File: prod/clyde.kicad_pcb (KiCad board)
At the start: 2 copper layers, 111.4 x 85.7 mm, 26 parts

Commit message: prototypes ordered
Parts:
- removed the G*** at (196.5, 151.8)
- removed the G*** at (196.4, 151.3)
- added G***: LOGO, main:north-sky-silk, F.Cu at (198.8, 149.9)
- added G***: LOGO, main:north-sky-silk, B.Cu at (198.8, 149.9)
- moved S16 1.91 mm to (206.7, 179.1)
- moved S17 1.91 mm to (225.7, 179.1)
- moved _4 1.91 mm to (235.3, 169.5)
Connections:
- TRRS1 pad 4: GP12 -> GP16
- U0 pad 10: matrix_middle_home -> matrix_inner_home
- U0 pad 11: matrix_middle_bottom -> matrix_inner_bottom
- U0 pad 12: matrix_index_top -> matrix_ring_bottom
- U0 pad 14: matrix_index_home -> matrix_ring_home
- U0 pad 15: matrix_index_bottom -> matrix_ring_top
- U0 pad 16: GP12 -> matrix_middle_top
- U0 pad 17: matrix_inner_bottom -> matrix_middle_home
- U0 pad 19: matrix_inner_home -> matrix_middle_bottom
- U0 pad 20: matrix_inner_top -> GP15
- U0 pad 21: thumbfan_far_home -> GP16
- U0 pad 22: thumbfan_home_home -> thumbfan_far_home
- U0 pad 24: thumbfan_near_home -> thumbfan_home_home
- U0 pad 25: GP19 -> thumbfan_near_home
- U0 pad 5: matrix_ring_bottom -> matrix_index_bottom
- U0 pad 6: matrix_ring_home -> matrix_index_home
- U0 pad 7: matrix_ring_top -> matrix_index_top
- U0 pad 9: matrix_middle_top -> matrix_inner_top
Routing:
- net GP16: track 0.00 -> 117.3 mm
- net GP12: track 114.2 -> 0.00 mm, vias 2 -> 0
- net matrix_inner_top: track 105.9 -> 140.8 mm
- net matrix_index_bottom: track 45.5 -> 78.3 mm
- net matrix_index_home: track 65.8 -> 93.8 mm, vias 2 -> 1
- net matrix_inner_home: track 90.1 -> 116.3 mm, vias 0 -> 1
- net thumbfan_far_home: track 107.0 -> 81.8 mm
- net matrix_ring_home: track 67.2 -> 48.4 mm
- net matrix_ring_bottom: track 50.1 -> 31.3 mm
- net matrix_inner_bottom: track 74.2 -> 92.9 mm, vias 0 -> 1
- net matrix_ring_top: track 84.2 -> 66.4 mm
- net matrix_index_top: track 90.6 -> 107.7 mm
- net thumbfan_home_home: track 78.5 -> 65.0 mm
- net matrix_middle_top: track 78.1 -> 66.6 mm
- net matrix_middle_home: track 57.2 -> 50.1 mm
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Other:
- outline, holes or cut-outs redrawn

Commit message: layout like split weteor/Kong; outline tweaks
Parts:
- removed the G*** at (198.8, 149.9) (x2)
- added G***: LOGO, main:north-sky-silk, F.Cu at (197.2, 151.8)
- added G***: LOGO, main:north-sky-silk, B.Cu at (197.0, 151.8)
- moved S16 4.76 mm to (209.6, 175.3)
- moved S17 4.76 mm to (228.6, 175.3)
- moved _4 4.76 mm to (238.1, 165.7)
- moved S18 4.39 mm to (247.7, 177.6)
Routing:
- net thumbfan_home_home: track 65.0 -> 88.8 mm
- net thumbfan_far_home: track 81.8 -> 95.3 mm
- net matrix_inner_bottom: track 92.9 -> 104.9 mm
- net matrix_index_top: track 107.7 -> 117.8 mm
- net matrix_inner_home: track 116.3 -> 124.6 mm
- net matrix_inner_top: track 140.8 -> 146.5 mm
- net matrix_index_home: track 93.8 -> 99.1 mm
- net thumbfan_near_home: track 67.8 -> 71.8 mm
- net matrix_ring_bottom: track 31.3 -> 35.3 mm
- net matrix_index_bottom: track 78.3 -> 81.8 mm
- net matrix_middle_top: track 66.6 -> 68.5 mm
- net matrix_middle_home: track 50.1 -> 48.5 mm
- net matrix_pinky_top: track 64.0 -> 65.4 mm
- net matrix_ring_top: track 66.4 -> 67.7 mm
- net matrix_middle_bottom: track 33.5 -> 34.7 mm
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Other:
- board size 111.4 x 85.7 mm -> 114.3 x 82.4 mm
- board text added: "clyde v0.0.2"
- board text removed: "clyde v0.0.1"

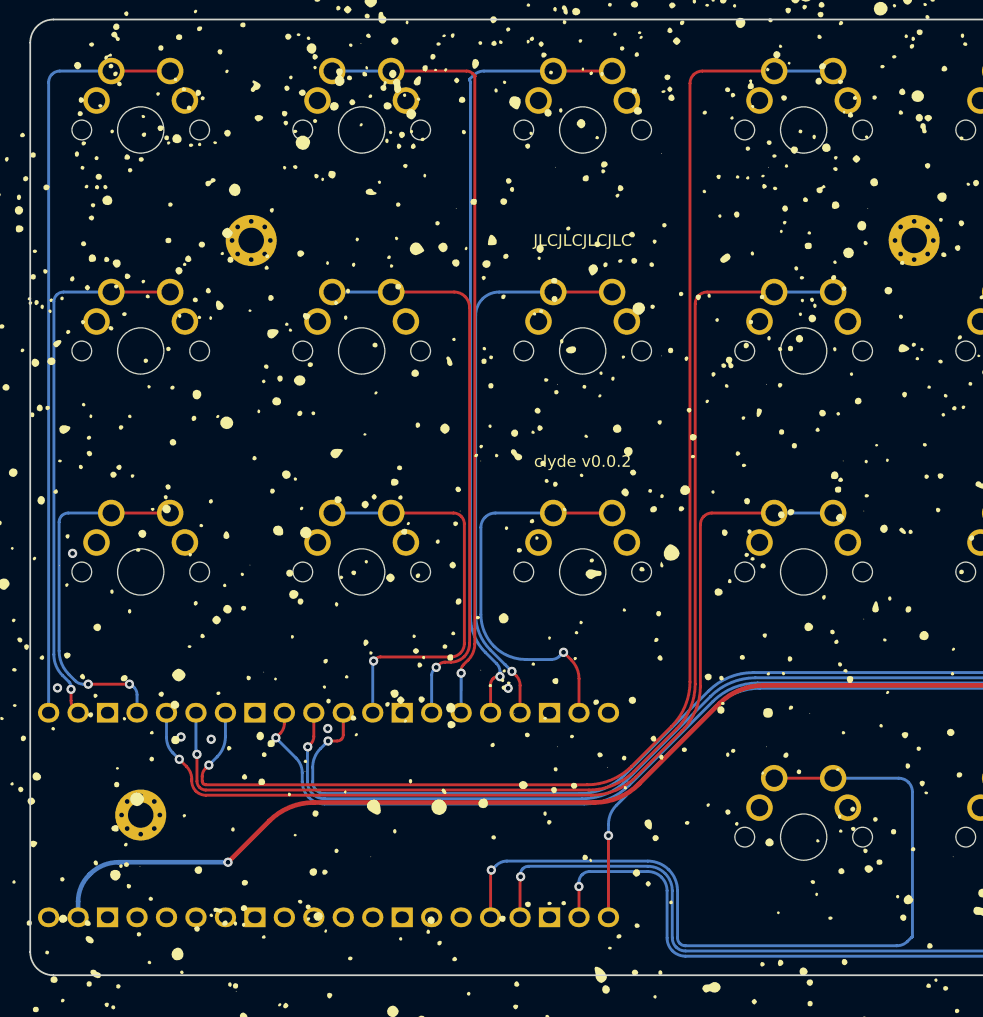
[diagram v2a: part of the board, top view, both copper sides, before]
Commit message: fix some routing irregularities
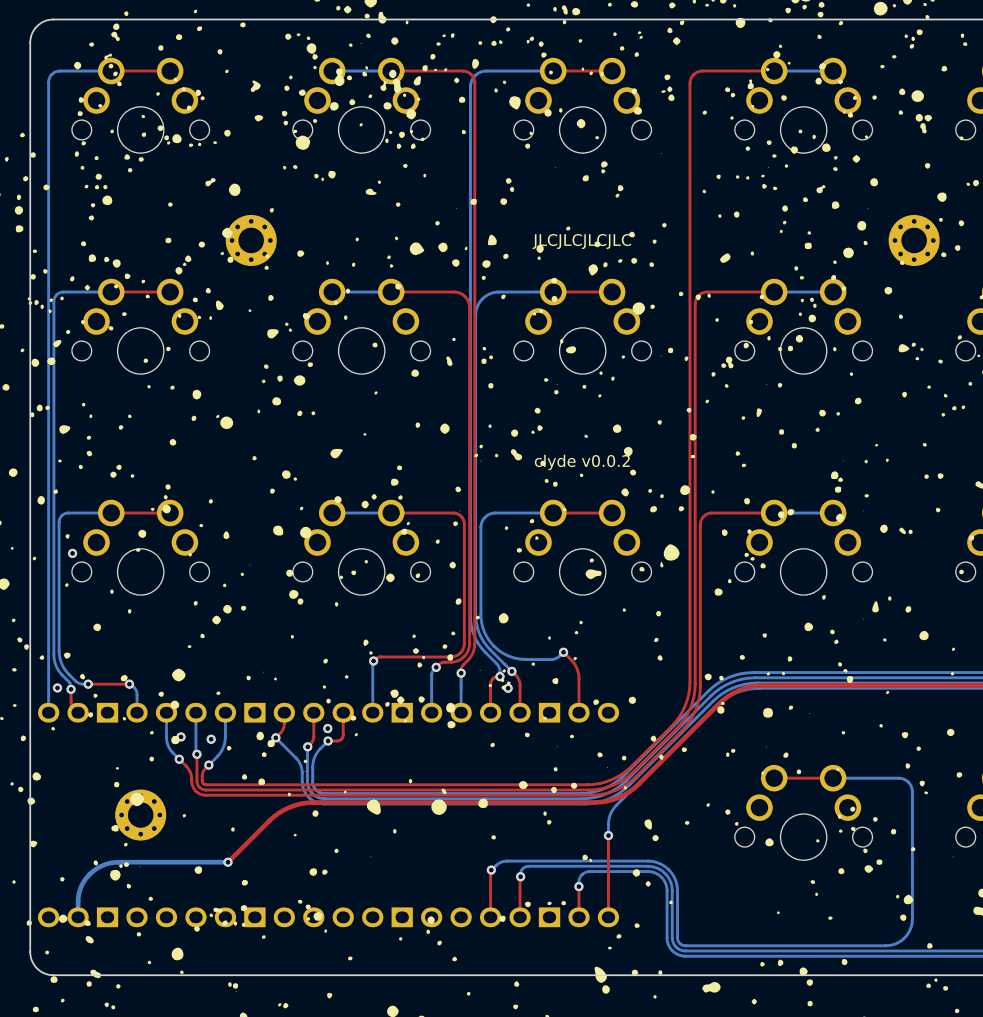
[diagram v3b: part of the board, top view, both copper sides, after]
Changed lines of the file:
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@@
   (segment (start 146.39375 162.51875) (end 146.39375 163.495798) (width 0.25) (layer "F.Cu") (net 3))
   (via (at 146.39375 162.51875) (size 0.8) (drill 0.4) (layers "F.Cu" "B.Cu") (net 3))
-  (arc (start 146.698125 164.230625) (mid 146.472854 163.893483) (end 146.39375 163.495798) (width 0.25) (layer "F.Cu") (net 3))
+  (arc (start 146.39375 163.495798) (mid 146.472854 163.893483) (end 146.698125 164.230625) (width 0.25) (layer "F.Cu") (net 3))
   (segment (start 146.39375 162.2875) (end 146.39375 162.51875) (width 0.25) (layer "B.Cu") (net 3))
   (segment (start 146.230231 161.892731) (end 145.653125 161.315625) (width 0.25) (layer "B.Cu") (net 3))
@@
   (segment (start 168.91 128.27) (end 173.99 128.27) (width 0.25) (layer "B.Cu") (net 6))
   (arc (start 177.67875 160.82125) (mid 177.533503 161.038626) (end 177.4825 161.295039) (width 0.25) (layer "B.Cu") (net 6))
+  (segment (start 180.1672 109.22) (end 173.99 109.22) (width 0.25) (layer "F.Cu") (net 7))
+  (segment (start 181.2 110.252799) (end 181.2 158.591941) (width 0.25) (layer "F.Cu") (net 7))
   (segment (start 180.612499 160.010291) (end 180.211396 160.411395) (width 0.25) (layer "F.Cu") (net 7))
-  (segment (start 181.2125 109.6375) (end 181.01 109.435) (width 0.25) (layer "F.Cu") (net 7))
-  (segment (start 181.2 109.692677) (end 181.2 158.591941) (width 0.25) (layer "F.Cu") (net 7))
   (segment (start 180.025 160.861396) (end 180.025 161.125) (width 0.25) (layer "F.Cu") (net 7))
-  (segment (start 180.490944 109.22) (end 173.99 109.22) (width 0.25) (layer "F.Cu") (net 7))
   (via (at 180.025 161.125) (size 0.8) (drill 0.4) (layers "F.Cu" "B.Cu") (net 7))
+  (arc (start 180.8975 109.5225) (mid 180.562435 109.298617) (end 180.1672 109.22) (width 0.25) (layer "F.Cu") (net 7))
+  (arc (start 180.211396 160.411395) (mid 180.073442 160.617857) (end 180.025 160.861396) (width 0.25) (layer "F.Cu") (net 7))
   (arc (start 180.612499 160.010291) (mid 181.047313 159.359546) (end 181.2 158.591941) (width 0.25) (layer "F.Cu") (net 7))
-  (arc (start 181.2125 109.6375) (mid 181.217677 109.65) (end 181.2125 109.6625) (width 0.25) (layer "F.Cu") (net 7))
-  (arc (start 180.211396 160.411395) (mid 180.073442 160.617857) (end 180.025 160.861396) (width 0.25) (layer "F.Cu") (net 7))
-  (arc (start 181.01 109.435) (mid 180.771855 109.275876) (end 180.490944 109.22) (width 0.25) (layer "F.Cu") (net 7))
-  (arc (start 181.2 109.692677) (mid 181.203248 109.676345) (end 181.2125 109.6625) (width 0.25) (layer "F.Cu") (net 7))
+  (arc (start 181.2 110.252799) (mid 181.121382 109.857564) (end 180.8975 109.5225) (width 0.25) (layer "F.Cu") (net 7))
   (segment (start 168.91 109.22) (end 173.99 109.22) (width 0.25) (layer "B.Cu") (net 7))
   (segment (start 180.025 161.125) (end 180.0225 164.535) (width 0.25) (layer "B.Cu") (net 7))
@@
   (arc (start 182.5625 162.086503) (mid 182.612853 161.833356) (end 182.756249 161.618749) (width 0.25) (layer "F.Cu") (net 10))
   (segment (start 182.1 159.322792) (end 183.082537 160.305329) (width 0.25) (layer "B.Cu") (net 10))
-  (segment (start 180.7625 109.9125) (end 181.0775 109.5975) (width 0.25) (layer "B.Cu") (net 10))
-  (segment (start 180.825 156.244669) (end 180.825 110.188388) (width 0.25) (layer "B.Cu") (net 10))
-  (segment (start 181.988865 109.22) (end 187.96 109.22) (width 0.25) (layer "B.Cu") (net 10))
+  (segment (start 180.825 110.60027) (end 180.825 156.244669) (width 0.25) (layer "B.Cu") (net 10))
   (segment (start 183.375 161.011396) (end 183.375 161.425) (width 0.25) (layer "B.Cu") (net 10))
-  (arc (start 181.988865 109.22) (mid 181.495637 109.318109) (end 181.0775 109.5975) (width 0.25) (layer "B.Cu") (net 10))
-  (arc (start 180.7625 109.9125) (mid 180.736611 109.975) (end 180.7625 110.0375) (width 0.25) (layer "B.Cu") (net 10))
-  (arc (start 180.7625 110.0375) (mid 180.808756 110.106728) (end 180.825 110.188388) (width 0.25) (layer "B.Cu") (net 10))
+  (segment (start 182.20527 109.22) (end 187.96 109.22) (width 0.25) (layer "B.Cu") (net 10))
   (arc (start 180.825 156.244669) (mid 181.156361 157.910537) (end 182.1 159.322792) (width 0.25) (layer "B.Cu") (net 10))
+  (arc (start 180.825 110.60027) (mid 180.930066 110.072063) (end 181.229272 109.624272) (width 0.25) (layer "B.Cu") (net 10))
   (arc (start 183.375 161.011396) (mid 183.298991 160.629275) (end 183.082537 160.305329) (width 0.25) (layer "B.Cu") (net 10))
+  (arc (start 181.229272 109.624272) (mid 181.677063 109.325066) (end 182.20527 109.22) (width 0.25) (layer "B.Cu") (net 10))
   (segment (start 158.018198 171.65) (end 191.246036 171.65) (width 0.25) (layer "F.Cu") (net 11))
   (segment (start 156.8 170.280698) (end 156.8 170.431801) (width 0.25) (layer "F.Cu") (net 11))
@@
   (via (at 182.625 178.1) (size 0.8) (drill 0.4) (layers "F.Cu" "B.Cu") (net 17))
   (arc (start 182.5625 178.206694) (mid 182.570621 178.165864) (end 182.59375 178.13125) (width 0.25) (layer "F.Cu") (net 17))
-  (segment (start 218.9125 183.8375) (end 218.910937 183.839062) (width 0.25) (layer "B.Cu") (net 17))
-  (segment (start 218.881249 183.868749) (end 218.879687 183.870312) (width 0.25) (layer "B.Cu") (net 17))
-  (segment (start 218.90625 183.84375) (end 218.9 183.85) (width 0.25) (layer "B.Cu") (net 17))
-  (segment (start 218.925 171.366439) (end 218.925 183.807322) (width 0.25) (layer "B.Cu") (net 17))
-  (segment (start 218.5125 184.2375) (end 218.8375 183.9125) (width 0.25) (layer "B.Cu") (net 17))
-  (segment (start 218.910937 183.839062) (end 218.907812 183.842187) (width 0.25) (layer "B.Cu") (net 17))
-  (segment (start 218.862499 183.887499) (end 218.870312 183.879687) (width 0.25) (layer "B.Cu") (net 17))
-  (segment (start 218.907812 183.842187) (end 218.90625 183.84375) (width 0.25) (layer "B.Cu") (net 17))
-  (segment (start 218.9 183.85) (end 218.89375 183.85625) (width 0.25) (layer "B.Cu") (net 17))
+  (segment (start 183.0375 177.7125) (end 182.65 178.1) (width 0.25) (layer "B.Cu") (net 17))
+  (segment (start 196.114339 177.325) (end 183.973007 177.325) (width 0.25) (layer "B.Cu") (net 17))
+  (segment (start 216.623806 184.625) (end 199.357842 184.625) (width 0.25) (layer "B.Cu") (net 17))
+  (segment (start 198.675 183.942157) (end 198.675 179.88566) (width 0.25) (layer "B.Cu") (net 17))
   (segment (start 217.73856 170.18) (end 212.09 170.18) (width 0.25) (layer "B.Cu") (net 17))
-  (segment (start 218.8875 183.8625) (end 218.881249 183.868749) (width 0.25) (layer "B.Cu") (net 17))
-  (segment (start 218.879687 183.870312) (end 218.870312 183.879687) (width 0.25) (layer "B.Cu") (net 17))
-  (segment (start 218.862499 183.887499) (end 218.8375 183.9125) (width 0.25) (layer "B.Cu") (net 17))
-  (segment (start 218.89375 183.85625) (end 218.8875 183.8625) (width 0.25) (layer "B.Cu") (net 17))
-  (segment (start 196.114339 177.325) (end 183.973007 177.325) (width 0.25) (layer "B.Cu") (net 17))
-  (segment (start 198.675 183.942157) (end 198.675 179.88566) (width 0.25) (layer "B.Cu") (net 17))
-  (segment (start 217.576992 184.625) (end 199.357842 184.625) (width 0.25) (layer "B.Cu") (net 17))
-  (segment (start 183.0375 177.7125) (end 182.65 178.1) (width 0.25) (layer "B.Cu") (net 17))
+  (segment (start 218.925 171.366439) (end 218.925 182.323806) (width 0.25) (layer "B.Cu") (net 17))
   (arc (start 196.114339 177.325) (mid 197.094261 177.519918) (end 197.925 178.075) (width 0.25) (layer "B.Cu") (net 17))
-  (arc (start 183.0375 177.7125) (mid 183.466714 177.425707) (end 183.973007 177.325) (width 0.25) (layer "B.Cu") (net 17))
-  (arc (start 218.5125 184.2375) (mid 218.083285 184.524292) (end 217.576992 184.625) (width 0.25) (layer "B.Cu") (net 17))
+  (arc (start 198.875 184.425) (mid 198.726978 184.203469) (end 198.675 183.942157) (width 0.25) (layer "B.Cu") (net 17))
+  (arc (start 218.250996 183.950996) (mid 217.504434 184.449832) (end 216.623806 184.625) (width 0.25) (layer "B.Cu") (net 17))
+  (arc (start 218.925 182.323806) (mid 218.749832 183.204434) (end 218.250996 183.950996) (width 0.25) (layer "B.Cu") (net 17))
+  (arc (start 198.875 184.425) (mid 199.096529 184.573021) (end 199.357842 184.625) (width 0.25) (layer "B.Cu") (net 17))
+  (arc (start 198.675 179.88566) (mid 198.480081 178.905737) (end 197.925 178.075) (width 0.25) (layer "B.Cu") (net 17))
   (arc (start 217.73856 170.18) (mid 218.192591 170.270312) (end 218.5775 170.5275) (width 0.25) (layer "B.Cu") (net 17))
   (arc (start 218.925 171.366439) (mid 218.834687 170.912408) (end 218.5775 170.5275) (width 0.25) (layer "B.Cu") (net 17))
-  (arc (start 198.875 184.425) (mid 198.726978 184.203469) (end 198.675 183.942157) (width 0.25) (layer "B.Cu") (net 17))
-  (arc (start 198.875 184.425) (mid 199.096529 184.573021) (end 199.357842 184.625) (width 0.25) (layer "B.Cu") (net 17))
-  (arc (start 218.9125 183.8375) (mid 218.921751 183.823654) (end 218.925 183.807322) (width 0.25) (layer "B.Cu") (net 17))
-  (arc (start 198.675 179.88566) (mid 198.480081 178.905737) (end 197.925 178.075) (width 0.25) (layer "B.Cu") (net 17))
+  (arc (start 183.0375 177.7125) (mid 183.466714 177.425707) (end 183.973007 177.325) (width 0.25) (layer "B.Cu") (net 17))
   (segment (start 185.12625 178.69875) (end 185.15 178.675) (width 0.25) (layer "F.Cu") (net 18))
   (segment (start 185.1025 178.756087) (end 185.1025 182.175) (width 0.25) (layer "F.Cu") (net 18))
